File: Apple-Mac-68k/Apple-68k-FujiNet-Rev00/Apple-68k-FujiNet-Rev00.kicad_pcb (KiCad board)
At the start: 2 copper layers, 80.8 x 70.6 mm, 28 parts, among them J1 Apple IDC-20, J2 Logic Analyzer, J3 UART, J4 SWD, P1 ST-TF-003A, SW1 ButtonA, SW2 Safe Reset, U1 Pico, U2 ESP32-S3-DevKitC-1 N16R8

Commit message: Drop redundant GND traces on Apple 68k Rev00
The ground pour already connects every GND pad; the only isolated piece
was the SD socket's G4 shield tab, now tied to the bottom pour with a
single via.

Co-Authored-By: Claude Opus 5.5 <noreply@anthropic.com>
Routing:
- net GND: track 361.2 -> 0.00 mm, vias 0 -> 1

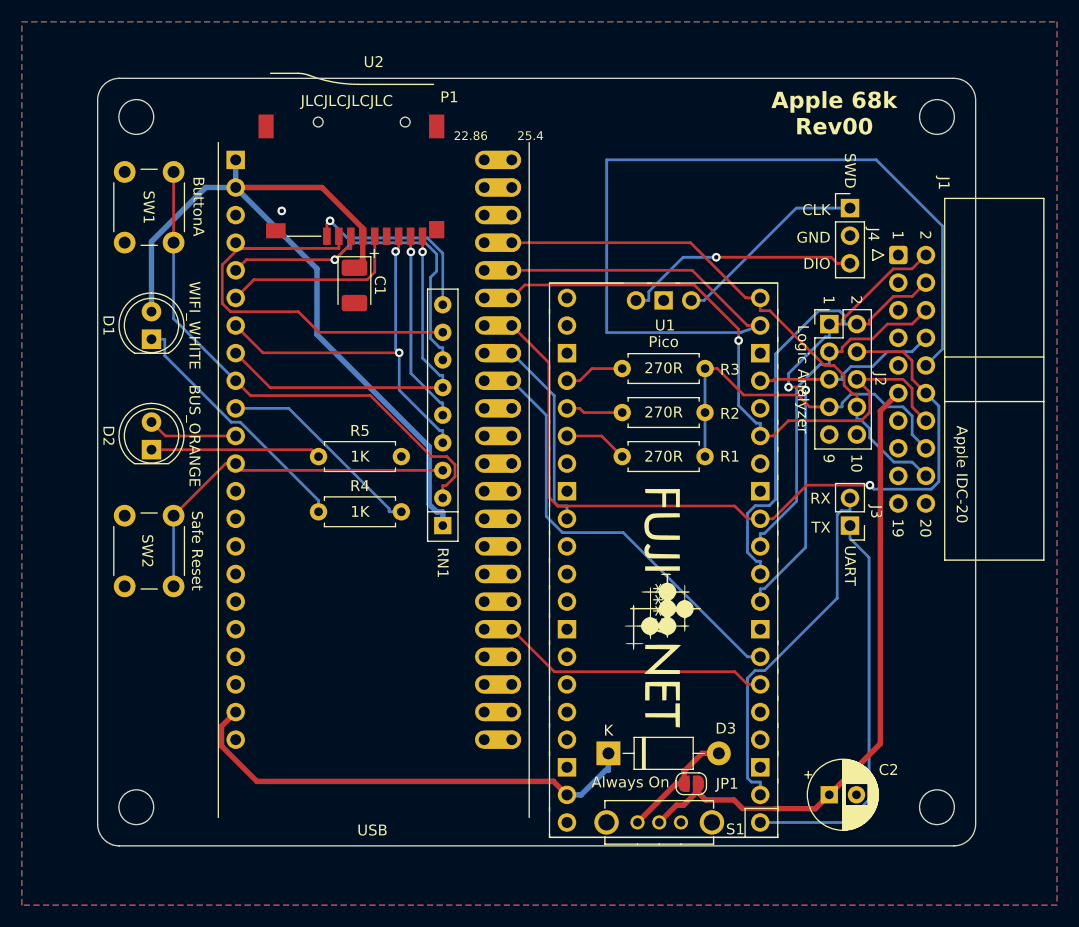
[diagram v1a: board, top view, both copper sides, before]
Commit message: Straighten autorouter jogs on Apple 68k Rev00
Merge 77 short pad-exit and mid-route doglegs into single segments,
keeping only replacements that hold clearance to other nets.

Co-Authored-By: Claude Opus 5.5 <noreply@anthropic.com>
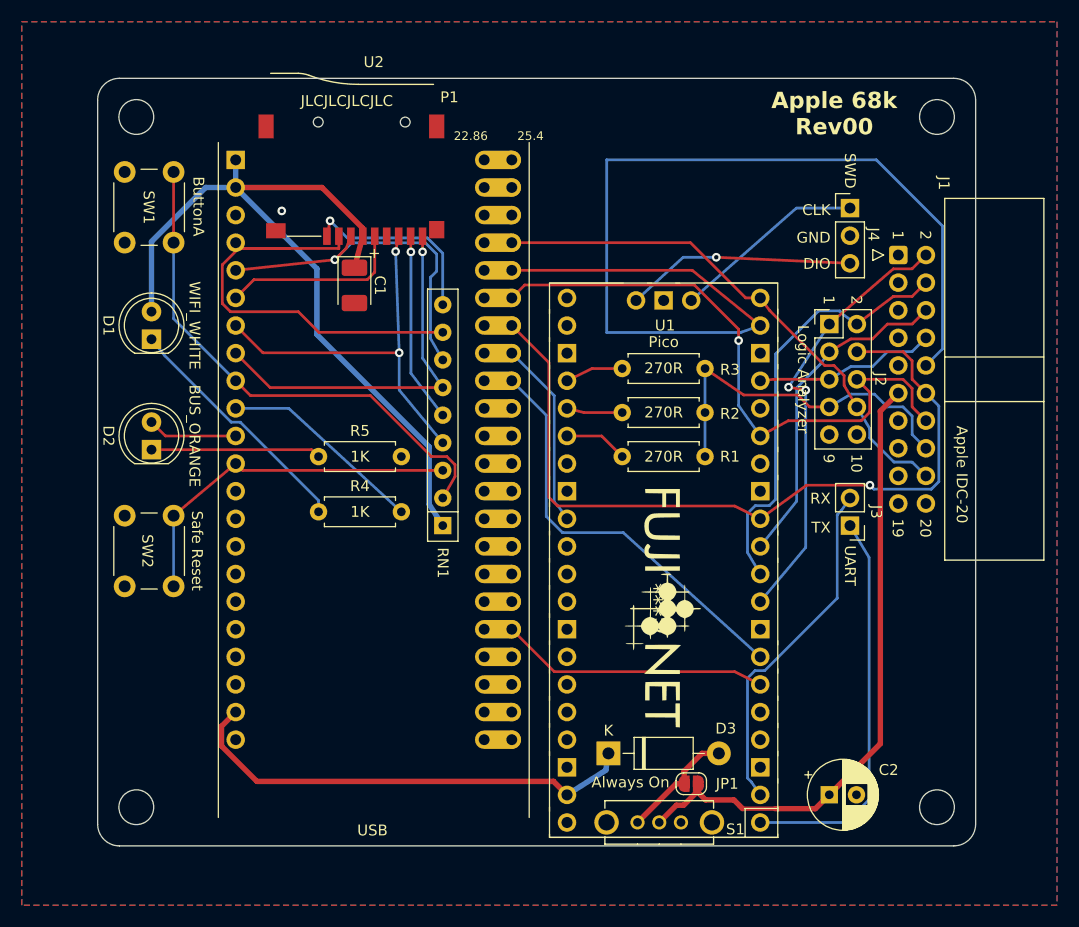
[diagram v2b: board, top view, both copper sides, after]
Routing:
- net /CA0: track 42.4 -> 40.8 mm
- net /CA2: track 31.9 -> 30.6 mm
- net /CA1: track 41.0 -> 39.7 mm
- net /WR_DATA: track 52.6 -> 51.3 mm
- net Net-(J3-Pin_2): track 33.2 -> 32.1 mm
- net /SPI_MOSI: track 33.6 -> 32.6 mm
- net Net-(D1-K): track 23.4 -> 22.7 mm
- net /SWDIO: track 22.0 -> 21.2 mm
- net +3.3V: track 75.3 -> 74.6 mm
- net /RD_DATA: track 33.6 -> 33.0 mm
- net /ENBL2: track 59.9 -> 59.2 mm
- net /SPI_MISO: track 37.2 -> 36.6 mm
- net /RMT_FROM_ESP: track 20.4 -> 19.8 mm
- net +5V: track 43.6 -> 43.1 mm

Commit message: Undo any-angle jog straightening on Apple 68k Rev00
Restore the 45-degree routing from before a5426cb; the merged segments
left traces at arbitrary angles. Also square up the last WREQ leg into
the Pico so every segment is a multiple of 45 degrees.

Co-Authored-By: Claude Opus 5.5 <noreply@anthropic.com>
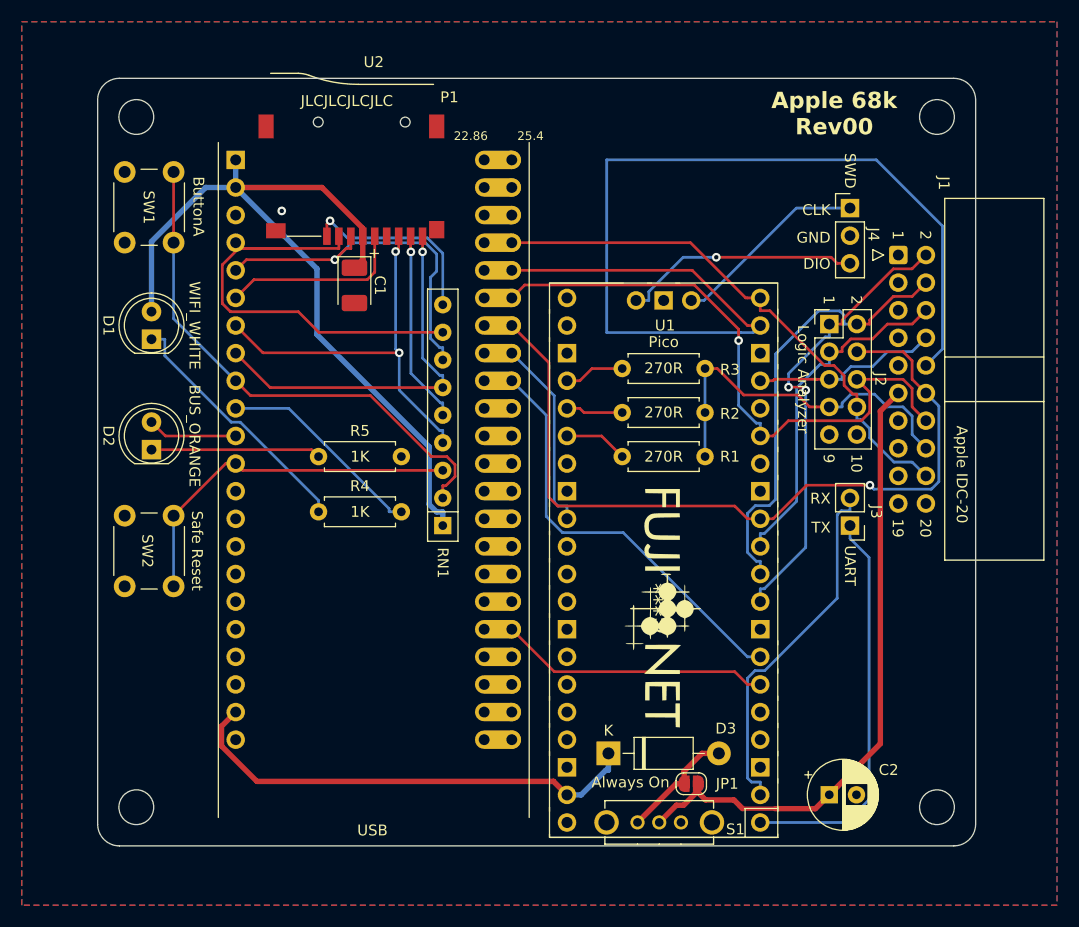
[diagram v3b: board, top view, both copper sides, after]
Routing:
- net /CA0: track 40.8 -> 42.4 mm
- net /CA2: track 30.6 -> 31.9 mm
- net /CA1: track 39.7 -> 41.0 mm
- net /WR_DATA: track 51.3 -> 52.6 mm
- net Net-(J3-Pin_2): track 32.1 -> 33.2 mm
- net /SPI_MOSI: track 32.6 -> 33.6 mm
- net Net-(D1-K): track 22.7 -> 23.4 mm
- net /SWDIO: track 21.2 -> 22.0 mm
- net +3.3V: track 74.6 -> 75.3 mm
- net /RD_DATA: track 33.0 -> 33.6 mm
- net /ENBL2: track 59.2 -> 59.9 mm
- net /SPI_MISO: track 36.6 -> 37.2 mm
- net /RMT_FROM_ESP: track 19.8 -> 20.4 mm
- net +5V: track 43.1 -> 43.6 mm
